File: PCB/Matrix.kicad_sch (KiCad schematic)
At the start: 133 parts, among them SW1 CPG151101S11, SW10 CPG151101S11, SW11 CPG151101S11, SW12 CPG151101S11, SW13 CPG151101S11, SW14 CPG151101S11, SW15 CPG151101S11, SW16 CPG151101S11, SW17 CPG151101S11, SW18 CPG151101S11, SW19 CPG151101S11, SW2 CPG151101S11, SW20 CPG151101S11, SW21 CPG151101S11, SW22 CPG151101S11, SW23 CPG151101S11, SW24 CPG151101S11, SW25 CPG151101S11, SW26 CPG151101S11, SW27 CPG151101S11, SW28 CPG151101S11, SW29 CPG151101S11, SW3 CPG151101S11, SW30 CPG151101S11, SW31 CPG151101S11, SW32 CPG151101S11, SW33 CPG151101S11, SW34 CPG151101S11, SW35 CPG151101S11, SW36 CPG151101S11, SW37 CPG151101S11, SW38 CPG151101S11, SW39 CPG151101S11, SW4 CPG151101S11, SW40 CPG151101S11, SW41 CPG151101S11, SW42 CPG151101S11, SW43 CPG151101S11, SW44 CPG151101S11, SW45 CPG151101S11, SW46 CPG151101S11, SW47 CPG151101S11, SW48 CPG151101S11, SW49 CPG151101S11, SW5 CPG151101S11, SW50 CPG151101S11, SW51 CPG151101S11, SW52 CPG151101S11, SW53 CPG151101S11, SW54 CPG151101S11, SW55 CPG151101S11, SW56 CPG151101S11, SW57 CPG151101S11, SW58 CPG151101S11, SW59 CPG151101S11, SW6 CPG151101S11, SW60 CPG151101S11, SW61 CPG151101S11, SW62 CPG151101S11, SW63 CPG151101S11, SW64 Encoder, SW7 CPG151101S11, SW8 CPG151101S11, SW9 CPG151101S11

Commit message: Added large caps to output of TPS2557. Updated STEP file and file data.
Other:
- company: (none) -> Created by Ariamelon (https://github.com/Ariamelon/Honeydew/)
- title: (none) -> Honeydew unified split ergonomic keyboard
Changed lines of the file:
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@@
   (paper "A4")
   (title_block
-    (date "2023-04-03")
+    (title "Honeydew unified split ergonomic keyboard")
+    (date "2023-04-08")
     (rev "V2.0")
+    (company "Created by Ariamelon (https://github.com/Ariamelon/Honeydew/)")
     (comment 1 "All capacitors 50V unless otherwise specified.")
+    (comment 2 "Licensed under CC BY 4.0.")
   )
   (junction (at 102.87 71.12) (diameter 0) (color 0 0 0 0)

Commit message: 17/04/2023 large update.
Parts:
- removed SW64: Encoder, Honeydew:PER60, symbol Device:RotaryEncoder
- added C95 (x2): 100n, Capacitor_SMD:C_0402_1005Metric, symbol Device:C_Small
- added D64: 1N4148, Honeydew:D_SOD-323, symbol Device:D_Small
- added SW64: CPG151101S11, Honeydew:MXOnly-2U-Hotswap, symbol Cantaloupe:SW_SPST_Small
- added SW65: PER56, Honeydew:PER56, symbol Device:RotaryEncoder
- added U10, U11: 74HC595, Honeydew:SOIC-16_3.9x9.9mm_P1.27mm, symbol 74xx:74HC595
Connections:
- net +3V3: now also C95.2, C95.2, U10.10 (~{SRCLR}), U10.16 (VCC), U11.10 (~{SRCLR}), U11.16 (VCC)
- net COL0: now also U10.7 (QH)
- net COL1: now also U10.6 (QG)
- net COL10: now also SW36.2 (B), SW37.2 (B), SW38.2 (B), SW39.2 (B), SW40.2 (B), U11.5 (QF); no longer SW51.2 (B), SW52.2 (B), SW53.2 (B), SW54.2 (B), SW55.2 (B)
- net COL11: now also SW41.2 (B), SW42.2 (B), SW43.2 (B), SW44.2 (B), SW45.2 (B), U11.4 (QE); no longer SW56.2 (B), SW57.2 (B), SW58.2 (B), SW59.2 (B), SW60.2 (B)
- net COL2: now also U10.5 (QF)
- net COL3: now also U10.4 (QE)
- net COL4: now also U10.3 (QD)
- net COL5: now also U10.1 (QB)
- net COL6: now also SW61.2 (B), U10.15 (QA); no longer SW31.2 (B), SW32.2 (B), SW33.2 (B), SW34.2 (B), SW35.2 (B)
- net COL7: now also SW62.2 (B), SW64.2 (B), U10.2 (QC); no longer SW36.2 (B), SW37.2 (B), SW38.2 (B), SW39.2 (B), SW40.2 (B)
- net COL8: now also SW63.2 (B), U11.7 (QH); no longer SW41.2 (B), SW42.2 (B), SW43.2 (B), SW44.2 (B), SW45.2 (B)
- net COL9: now also SW31.2 (B), SW32.2 (B), SW33.2 (B), SW34.2 (B), SW35.2 (B), U11.6 (QG); no longer SW46.2 (B), SW47.2 (B), SW48.2 (B), SW49.2 (B), SW50.2 (B)
- net GND: now also C95.1, C95.1, SW65.C, U10.13 (~{OE}), U10.8 (GND), U11.13 (~{OE}), U11.8 (GND)
- net ROW2: no longer D61.1 (K)
- net ROW3: now also D61.1 (K), D63.1 (K)
- net ROW4: now also D64.1 (K); no longer D63.1 (K)
- net at C1.2, R1.2, R2.1: now also SW65.A
- net at C2.2, R3.2, R4.1: now also SW65.B
- removed net COLM: SW61.2 (B), SW62.2 (B), SW63.2 (B)
- new net: D64.2 (A), SW64.1 (A)
- new net: U10.9 (QH'), U11.14 (SER)
- new net COL12: SW46.2 (B), SW47.2 (B), SW48.2 (B), SW49.2 (B), SW50.2 (B), U11.3 (QD)
- new net COL13: SW51.2 (B), SW52.2 (B), SW53.2 (B), SW54.2 (B), SW55.2 (B), U11.2 (QC)
- new net COL14: SW56.2 (B), SW57.2 (B), SW58.2 (B), SW59.2 (B), SW60.2 (B), U11.1 (QB)
- new net MATRIX_CS: U10.12 (RCLK), U11.12 (RCLK)
- new net MOSI: U10.14 (SER)
- new net SCK: U10.11 (SRCLK), U11.11 (SRCLK)
- no-connect marks 0 -> 2
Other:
- moved on the sheet: C1, C2, D61, D62, D63, R1, R2, R3, R4, SW61, SW62, SW63

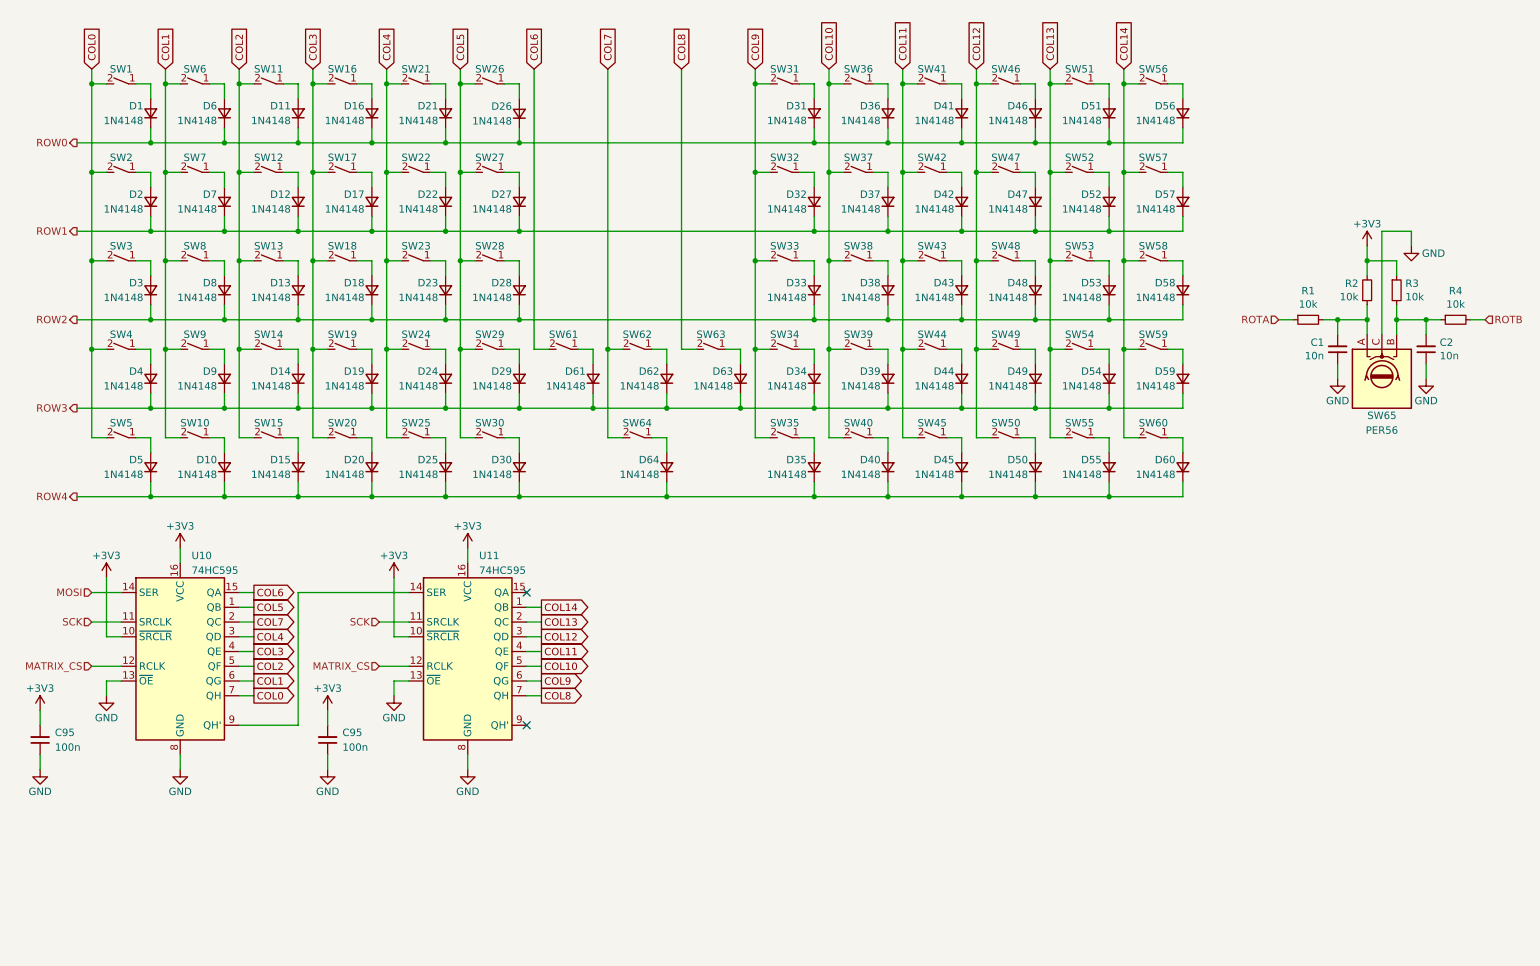
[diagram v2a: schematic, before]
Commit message: 3/4-done update.
Added current and voltage measurement for VBUS in and current measurement for the RGB output. Added PMOS power switch to fully turn off RGB LEDs when not in use. Rerouted the PCB. Moved OLED ribbon cable cutout and expanded it length-wise. Changed position of various components for better routing. Changed bulk capacitance of RGB LEDs to 5 x 22u capacitors. Changed the four N mosfets to two much smaller dual N mosfets. Still need to do RGB routing!
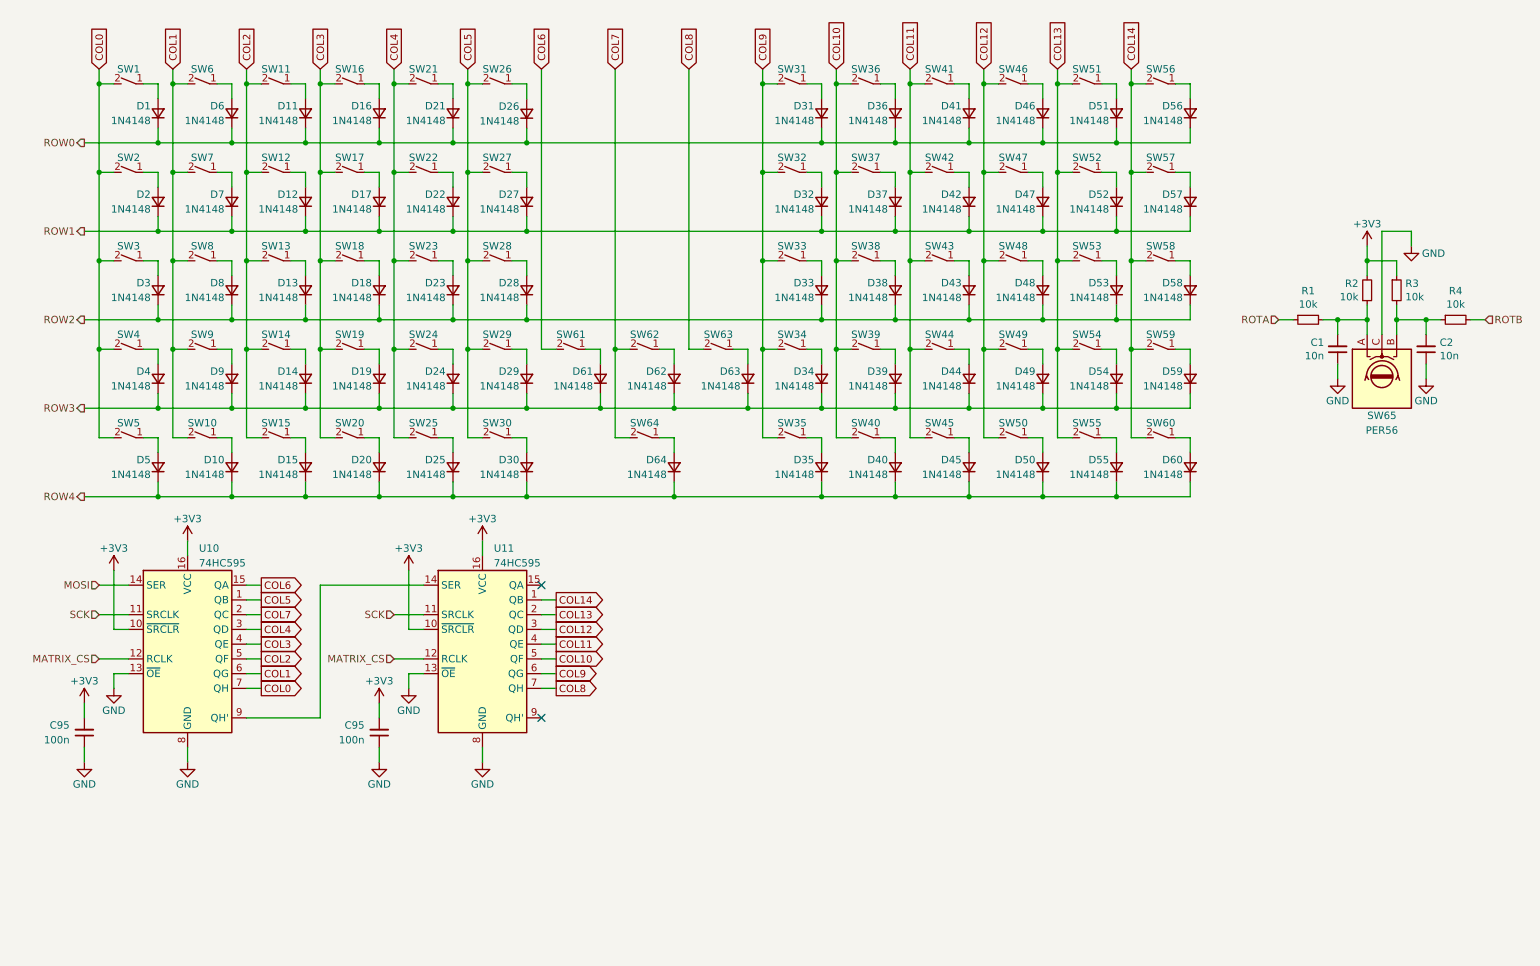
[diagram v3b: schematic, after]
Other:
- moved on the sheet: C95, D1, D10, D11, D12, D13, D14, D15, D16, D17, D18, D19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

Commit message: 05/05/2023 update.
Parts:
- added D64, D66: 1N4148, Honeydew:D_SOD-323, symbol Device:D_Small
- added SW64, SW66: CPG151101S11, Honeydew:MXOnly-1U-Hotswap, symbol Cantaloupe:SW_SPST_Small
- renumbered D64 to D65, SW64 to SW65, SW65 to SW67
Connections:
- net COL6: now also SW64.2 (B)
- net COL8: now also SW66.2 (B)
- net ROW4: now also D64.1 (K), D66.1 (K)
- new net: D64.2 (A), SW64.1 (A)
- new net: D66.2 (A), SW66.1 (A)

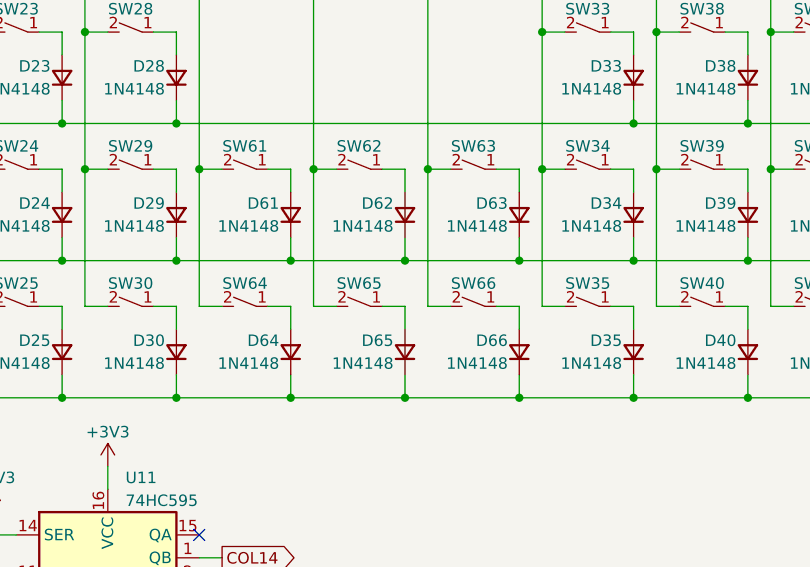
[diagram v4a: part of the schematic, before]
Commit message: Finished routing RGB LEDs.
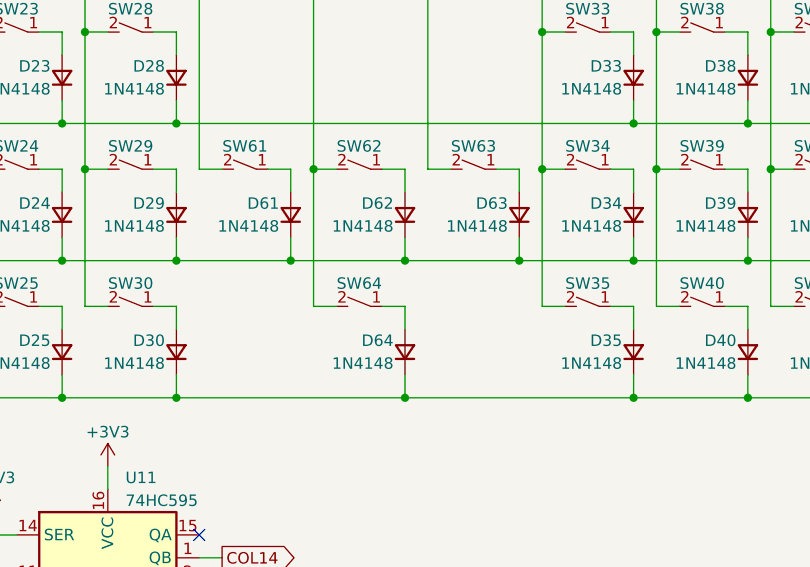
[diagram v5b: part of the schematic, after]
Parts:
- removed D64, D66: 1N4148, Honeydew:D_SOD-323, symbol Device:D_Small
- removed SW64, SW66: CPG151101S11, Honeydew:MXOnly-1U-Hotswap, symbol Cantaloupe:SW_SPST_Small
- renumbered D65 to D64, SW65 to SW64
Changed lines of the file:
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@@
   (junction (at 205.74 71.12) (diameter 0) (color 0 0 0 0)
   )
-  (junction (at 129.54 71.12) (diameter 0) (color 0 0 0 0)
-  )
   (junction (at 180.34 55.88) (diameter 0) (color 0 0 0 0)
   )
@@
   (junction (at 177.8 96.52) (diameter 0) (color 0 0 0 0)
   )
-  (junction (at 104.14 71.12) (diameter 0) (color 0 0 0 0)
-  )
   (junction (at 193.04 40.64) (diameter 0) (color 0 0 0 0)
   )
-  (junction (at 139.7 96.52) (diameter 0) (color 0 0 0 0)
-  )
   (junction (at 27.94 55.88) (diameter 0) (color 0 0 0 0)
   )
@@
   (junction (at 139.7 81.28) (diameter 0) (color 0 0 0 0)
   )
-  (junction (at 114.3 96.52) (diameter 0) (color 0 0 0 0)
-  )
   (junction (at 193.04 25.4) (diameter 0) (color 0 0 0 0)
   )
@@
     (stroke (width 0) (type default))
   )
-  (wire (pts (xy 114.3 93.98) (xy 114.3 96.52))
-    (stroke (width 0) (type default))
-  )
   (wire (pts (xy 215.9 27.94) (xy 215.9 25.4))
     (stroke (width 0) (type default))
@@
     (stroke (width 0) (type default))
   )
-  (wire (pts (xy 139.7 96.52) (xy 152.4 96.52))
+  (wire (pts (xy 127 96.52) (xy 152.4 96.52))
     (stroke (width 0) (type default))
   )
@@
     (stroke (width 0) (type default))
   )
-  (wire (pts (xy 101.6 96.52) (xy 114.3 96.52))
-    (stroke (width 0) (type default))
-  )
   (wire (pts (xy 116.84 86.36) (xy 119.38 86.36))
     (stroke (width 0) (type default))
@@
     (stroke (width 0) (type default))
   )
-  (wire (pts (xy 111.76 86.36) (xy 114.3 86.36))
-    (stroke (width 0) (type default))
-  )
   (wire (pts (xy 81.28 109.22) (xy 81.28 119.38))
     (stroke (width 0) (type default))
@@
     (stroke (width 0) (type default))
   )
-  (wire (pts (xy 137.16 86.36) (xy 139.7 86.36))
-    (stroke (width 0) (type default))
-  )
   (wire (pts (xy 88.9 88.9) (xy 88.9 86.36))
     (stroke (width 0) (type default))
@@
     (stroke (width 0) (type default))
   )
-  (wire (pts (xy 104.14 71.12) (xy 104.14 86.36))
-    (stroke (width 0) (type default))
-  )
   (wire (pts (xy 25.4 66.04) (xy 38.1 66.04))
     (stroke (width 0) (type default))
@@
     (stroke (width 0) (type default))
   )
-  (wire (pts (xy 129.54 86.36) (xy 132.08 86.36))
-    (stroke (width 0) (type default))
-  )
   (wire (pts (xy 27.94 40.64) (xy 30.48 40.64))
     (stroke (width 0) (type default))
@@
     (stroke (width 0) (type default))
   )
-  (wire (pts (xy 129.54 71.12) (xy 129.54 86.36))
-    (stroke (width 0) (type default))
-  )
   (wire (pts (xy 27.94 40.64) (xy 27.94 55.88))
     (stroke (width 0) (type default))
@@
     (stroke (width 0) (type default))
   )
-  (wire (pts (xy 114.3 96.52) (xy 127 96.52))
+  (wire (pts (xy 101.6 96.52) (xy 127 96.52))
     (stroke (width 0) (type default))
   )
@@
     (stroke (width 0) (type default))
   )
-  (wire (pts (xy 139.7 93.98) (xy 139.7 96.52))
-    (stroke (width 0) (type default))
-  )
   (wire (pts (xy 177.8 81.28) (xy 177.8 78.74))
     (stroke (width 0) (type default))
@@
     (stroke (width 0) (type default))
   )
-  (wire (pts (xy 114.3 88.9) (xy 114.3 86.36))
-    (stroke (width 0) (type default))
-  )
   (wire (pts (xy 76.2 73.66) (xy 76.2 71.12))
     (stroke (width 0) (type default))
@@
     (stroke (width 0) (type default))
   )
-  (wire (pts (xy 127 96.52) (xy 139.7 96.52))
-    (stroke (width 0) (type default))
-  )
   (wire (pts (xy 50.8 40.64) (xy 48.26 40.64))
     (stroke (width 0) (type default))
@@
     (stroke (width 0) (type default))
   )
-  (wire (pts (xy 104.14 86.36) (xy 106.68 86.36))
-    (stroke (width 0) (type default))
-  )
   (wire (pts (xy 93.98 71.12) (xy 91.44 71.12))
     (stroke (width 0) (type default))
@@
     (stroke (width 0) (type default))
   )
-  (wire (pts (xy 139.7 88.9) (xy 139.7 86.36))
-    (stroke (width 0) (type default))
-  )
   (wire (pts (xy 101.6 93.98) (xy 101.6 96.52))
     (stroke (width 0) (type default))
@@
     )
   )
-  (symbol (lib_id "Device:D_Small") (at 114.3 91.44 90) (unit 1)
-    (in_bom yes) (on_board yes) (dnp no)
-    (property "Reference" "D64" (at 113.03 90.17 90)
-      (effects (font (size 1.27 1.27)) (justify left))
-    )
-    (property "Value" "1N4148" (at 113.03 92.71 90)
-      (effects (font (size 1.27 1.27)) (justify left))
-    )
-    (property "Footprint" "Honeydew:D_SOD-323" (at 114.3 91.44 90)
-      (effects (font (size 1.27 1.27)) hide)
-    )
-    (property "Datasheet" "" (at 114.3 91.44 90)
-      (effects (font (size 1.27 1.27)) hide)
-    )
-    (property "Description" "SOD-323 diode" (at 114.3 91.44 0)
-      (effects (font (size 1.27 1.27)) hide)
-    )
-    (property "LCSC" "C2128" (at 114.3 91.44 0)
-      (effects (font (size 1.27 1.27)) hide)
-    )
-    (pin "1")
-    (pin "2")
-    (instances
-      (project "Honeydew"
-        (path "/534caec7-cf60-4f90-b1ed-42c9d445ef0f/c1819a82-630d-421e-8b73-d65ee471609e"
-          (reference "D64") (unit 1)
-        )
-      )
-    )
-  )
   (symbol (lib_id "Cantaloupe:SW_SPST_Small") (at 147.32 55.88 0) (mirror y) (unit 1)
     (in_bom yes) (on_board yes) (dnp no)
@@
     )
   )
-  (symbol (lib_id "Cantaloupe:SW_SPST_Small") (at 134.62 86.36 0) (mirror y) (unit 1)
-    (in_bom yes) (on_board yes) (dnp no)
-    (property "Reference" "SW66" (at 134.62 83.82 0)
-      (effects (font (size 1.27 1.27)))
-    )
-    (property "Value" "CPG151101S11" (at 134.62 93.98 0)
-      (effects (font (size 1.524 1.524)) hide)
-    )
-    (property "Footprint" "Honeydew:MXOnly-1U-Hotswap" (at 134.62 81.28 0)
-      (effects (font (size 1.524 1.524)) hide)
-    )
-    (property "Datasheet" "" (at 134.62 81.28 0)
-      (effects (font (size 1.524 1.524)) hide)
-    )
-    (property "Description" "Kailh hotswap sockets" (at 134.62 86.36 0)
-      (effects (font (size 1.27 1.27)) hide)
-    )
-    (property "LCSC" "C5184526" (at 134.62 86.36 0)
-      (effects (font (size 1.27 1.27)) hide)
-    )
-    (pin "1")
-    (pin "2")
-    (instances
-      (project "Honeydew"
-        (path "/534caec7-cf60-4f90-b1ed-42c9d445ef0f/c1819a82-630d-421e-8b73-d65ee471609e"
-          (reference "SW66") (unit 1)
-        )
-      )
-    )
-  )
   (symbol (lib_id "Device:D_Small") (at 152.4 91.44 90) (unit 1)
     (in_bom yes) (on_board yes) (dnp no)
@@
   (symbol (lib_id "Cantaloupe:SW_SPST_Small") (at 121.92 86.36 0) (mirror y) (unit 1)
     (in_bom yes) (on_board yes) (dnp no)
-    (property "Reference" "SW65" (at 121.92 83.82 0)
+    (property "Reference" "SW64" (at 121.92 83.82 0)
       (effects (font (size 1.27 1.27)))
     )
@@
       (project "Honeydew"
         (path "/534caec7-cf60-4f90-b1ed-42c9d445ef0f/c1819a82-630d-421e-8b73-d65ee471609e"
-          (reference "SW65") (unit 1)
+          (reference "SW64") (unit 1)
         )
       )
@@
     )
   )
-  (symbol (lib_id "Device:D_Small") (at 139.7 91.44 90) (unit 1)
-    (in_bom yes) (on_board yes) (dnp no)
-    (property "Reference" "D66" (at 138.43 90.17 90)
-      (effects (font (size 1.27 1.27)) (justify left))
-    )
-    (property "Value" "1N4148" (at 138.43 92.71 90)
-      (effects (font (size 1.27 1.27)) (justify left))
-    )
-    (property "Footprint" "Honeydew:D_SOD-323" (at 139.7 91.44 90)
-      (effects (font (size 1.27 1.27)) hide)
-    )
-    (property "Datasheet" "" (at 139.7 91.44 90)
-      (effects (font (size 1.27 1.27)) hide)
-    )
-    (property "Description" "SOD-323 diode" (at 139.7 91.44 0)
-      (effects (font (size 1.27 1.27)) hide)
-    )
-    (property "LCSC" "C2128" (at 139.7 91.44 0)
-      (effects (font (size 1.27 1.27)) hide)
-    )
-    (pin "1")
-    (pin "2")
-    (instances
-      (project "Honeydew"
-        (path "/534caec7-cf60-4f90-b1ed-42c9d445ef0f/c1819a82-630d-421e-8b73-d65ee471609e"
-          (reference "D66") (unit 1)
-        )
-      )
-    )
-  )
   (symbol (lib_id "Device:D_Small") (at 50.8 60.96 90) (unit 1)
     (in_bom yes) (on_board yes) (dnp no)
@@
     )
   )
-  (symbol (lib_id "Cantaloupe:SW_SPST_Small") (at 109.22 86.36 0) (mirror y) (unit 1)
-    (in_bom yes) (on_board yes) (dnp no)
-    (property "Reference" "SW64" (at 109.22 83.82 0)
-      (effects (font (size 1.27 1.27)))
-    )
-    (property "Value" "CPG151101S11" (at 109.22 93.98 0)
-      (effects (font (size 1.524 1.524)) hide)
-    )
-    (property "Footprint" "Honeydew:MXOnly-1U-Hotswap" (at 109.22 81.28 0)
-      (effects (font (size 1.524 1.524)) hide)
-    )
-    (property "Datasheet" "" (at 109.22 81.28 0)
-      (effects (font (size 1.524 1.524)) hide)
-    )
-    (property "Description" "Kailh hotswap sockets" (at 109.22 86.36 0)
-      (effects (font (size 1.27 1.27)) hide)
-    )
-    (property "LCSC" "C5184526" (at 109.22 86.36 0)
-      (effects (font (size 1.27 1.27)) hide)
-    )
-    (pin "1")
-    (pin "2")
-    (instances
-      (project "Honeydew"
-        (path "/534caec7-cf60-4f90-b1ed-42c9d445ef0f/c1819a82-630d-421e-8b73-d65ee471609e"
-          (reference "SW64") (unit 1)
-        )
-      )
-    )
-  )
   (symbol (lib_id "Cantaloupe:SW_SPST_Small") (at 172.72 40.64 0) (mirror y) (unit 1)
     (in_bom yes) (on_board yes) (dnp no)
@@
   (symbol (lib_id "Device:D_Small") (at 127 91.44 90) (unit 1)
     (in_bom yes) (on_board yes) (dnp no)
-    (property "Reference" "D65" (at 125.73 90.17 90)
+    (property "Reference" "D64" (at 125.73 90.17 90)
       (effects (font (size 1.27 1.27)) (justify left))
     )
@@
       (project "Honeydew"
         (path "/534caec7-cf60-4f90-b1ed-42c9d445ef0f/c1819a82-630d-421e-8b73-d65ee471609e"
-          (reference "D65") (unit 1)
+          (reference "D64") (unit 1)
         )
       )
